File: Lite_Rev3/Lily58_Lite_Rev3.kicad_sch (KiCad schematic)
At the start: 118 parts, among them J1 M2HOLE, J10 LOGO, J10 M2HOLE, J11 LOGO, J11 M2HOLE, J12 HOLE, J13 HOLE, J14 HOLE, J15 HOLE, J16 OLED_R, J19 breakaway, J2 M2HOLE, J20 breakaway, J21 breakaway, J22 AudioJack4, J22 breakaway, J3 HOLE, J4 HOLE, J5 HOLE, J6 HOLE, J7 OLED_L, J9 AudioJack4, SW1 SW_Push, SW10 SW_Push, SW11 SW_Push, SW12 SW_Push, SW13 SW_Push, SW14 SW_Push, SW15 SW_Push, SW16 SW_Push, SW17 SW_Push, SW18 SW_Push, SW19 SW_Push, SW2 SW_Push, SW20 SW_Push, SW21 SW_Push, SW22 SW_Push, SW23 SW_Push, SW24 SW_Push, SW25 SW_Push, SW26 SW_Push, SW27 SW_Push, SW28 SW_Push, SW29 SW_Push, SW3 SW_Push, SW30 SW_Push, SW31 SW_Push, SW32 SW_Push, SW33 SW_Push, SW34 SW_Push, SW35 SW_Push, SW36 SW_Push, SW37 SW_Push, SW38 SW_Push, SW39 SW_Push, SW4 SW_Push, SW40 SW_Push, SW41 SW_Push, SW42 SW_Push, SW43 SW_Push, SW44 SW_Push, SW45 SW_Push, SW46 SW_Push, SW47 SW_Push, SW48 SW_Push, SW49 SW_Push, SW5 SW_Push, SW50 SW_Push, SW51 SW_Push, SW52 SW_Push, SW53 SW_Push, SW54 SW_Push, SW55 SW_Push, SW56 SW_Push, SW57 SW_Push, SW58 SW_Push, SW6 SW_Push, SW7 SW_Push, SW8 SW_Push, SW9 SW_Push

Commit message: [Lily58 Lite Rev3] fix PCB
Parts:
- J12, J13, J14, J15, J3, J4, J5, J6: footprint yuchi:HOLE_M2_TH_5mm -> yuchi:HOLE_M2_TH
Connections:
- net COL4_L: now also SW11.1, SW17.1, SW23.1, SW29.1, SW5.1
- net LED_L_LV: now reaches U1.2 (GP2)
- net LED_R: now reaches U2.2 (GP2)
- no-connect marks 35 -> 33
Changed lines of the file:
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@@
   (title_block
     (title "Lily58 Lite Rev3")
-    (date "2024-09-07")
+    (date "2024-07-18")
   )
   (junction (at 160.02 166.37) (diameter 0) (color 0 0 0 0)
@@
   (no_connect (at 76.2 262.89))
   (no_connect (at 93.98 124.46))
-  (no_connect (at 109.22 162.56))
   (no_connect (at 80.01 46.99))
   (no_connect (at 76.2 170.18))
@@
   (no_connect (at 92.71 243.84))
   (no_connect (at 101.6 243.84))
-  (no_connect (at 113.03 39.37))
   (no_connect (at 85.09 124.46))
   (no_connect (at 93.98 271.78))
@@
     )
   )
+  (global_label "LED_R" (shape input) (at 109.22 162.56 0)
+    (effects (font (size 1.27 1.27)) (justify left))
+    (property "Intersheetrefs" "${INTERSHEET_REFS}" (at 109.22 162.56 0)
+      (effects (font (size 1.27 1.27)) hide)
+    )
+  )
   (global_label "TX_R" (shape input) (at 109.22 160.02 0) (fields_autoplaced)
     (effects (font (size 1.27 1.27)) (justify left))
@@
     )
   )
+  (global_label "COL4_L" (shape input) (at 240.03 34.29 90) (fields_autoplaced)
+    (effects (font (size 1.27 1.27)) (justify left))
+    (property "Intersheetrefs" "${INTERSHEET_REFS}" (at 240.03 24.471 90)
+      (effects (font (size 1.27 1.27)) (justify left) hide)
+    )
+  )
+  (global_label "LED_L_LV" (shape input) (at 113.03 39.37 0)
+    (effects (font (size 1.27 1.27)) (justify left))
+    (property "Intersheetrefs" "${INTERSHEET_REFS}" (at 113.03 39.37 0)
+      (effects (font (size 1.27 1.27)) hide)
+    )
+  )
   (global_label "ROW4_R" (shape input) (at 97.79 189.23 270)
     (effects (font (size 1.27 1.27)) (justify right))
@@
       (effects (font (size 1.27 1.27)) (justify right))
     )
-    (property "Footprint" "yuchi:HOLE_M2_TH_5mm" (at 92.71 238.76 0)
+    (property "Footprint" "yuchi:HOLE_M2_TH" (at 92.71 238.76 0)
       (effects (font (size 1.27 1.27)) hide)
     )
@@
       (effects (font (size 1.27 1.27)) (justify right))
     )
-    (property "Footprint" "yuchi:HOLE_M2_TH_5mm" (at 102.87 119.38 0)
+    (property "Footprint" "yuchi:HOLE_M2_TH" (at 102.87 119.38 0)
       (effects (font (size 1.27 1.27)) hide)
     )
@@
       (effects (font (size 1.27 1.27)) (justify right))
     )
-    (property "Footprint" "yuchi:HOLE_M2_TH_5mm" (at 83.82 238.76 0)
+    (property "Footprint" "yuchi:HOLE_M2_TH" (at 83.82 238.76 0)
       (effects (font (size 1.27 1.27)) hide)
     )
@@
       (effects (font (size 1.27 1.27)) (justify right))
     )
-    (property "Footprint" "yuchi:HOLE_M2_TH_5mm" (at 76.2 119.38 0)
+    (property "Footprint" "yuchi:HOLE_M2_TH" (at 76.2 119.38 0)
       (effects (font (size 1.27 1.27)) hide)
     )
@@
       (effects (font (size 1.27 1.27)) (justify right))
     )
-    (property "Footprint" "yuchi:HOLE_M2_TH_5mm" (at 74.93 238.76 0)
+    (property "Footprint" "yuchi:HOLE_M2_TH" (at 74.93 238.76 0)
       (effects (font (size 1.27 1.27)) hide)
     )
@@
       (effects (font (size 1.27 1.27)) (justify right))
     )
-    (property "Footprint" "yuchi:HOLE_M2_TH_5mm" (at 93.98 119.38 0)
+    (property "Footprint" "yuchi:HOLE_M2_TH" (at 93.98 119.38 0)
       (effects (font (size 1.27 1.27)) hide)
     )
@@
       (effects (font (size 1.27 1.27)) (justify right))
     )
-    (property "Footprint" "yuchi:HOLE_M2_TH_5mm" (at 85.09 119.38 0)
+    (property "Footprint" "yuchi:HOLE_M2_TH" (at 85.09 119.38 0)
       (effects (font (size 1.27 1.27)) hide)
     )
@@
       (effects (font (size 1.27 1.27)) (justify right))
     )
-    (property "Footprint" "yuchi:HOLE_M2_TH_5mm" (at 101.6 238.76 0)
+    (property "Footprint" "yuchi:HOLE_M2_TH" (at 101.6 238.76 0)
       (effects (font (size 1.27 1.27)) hide)
     )

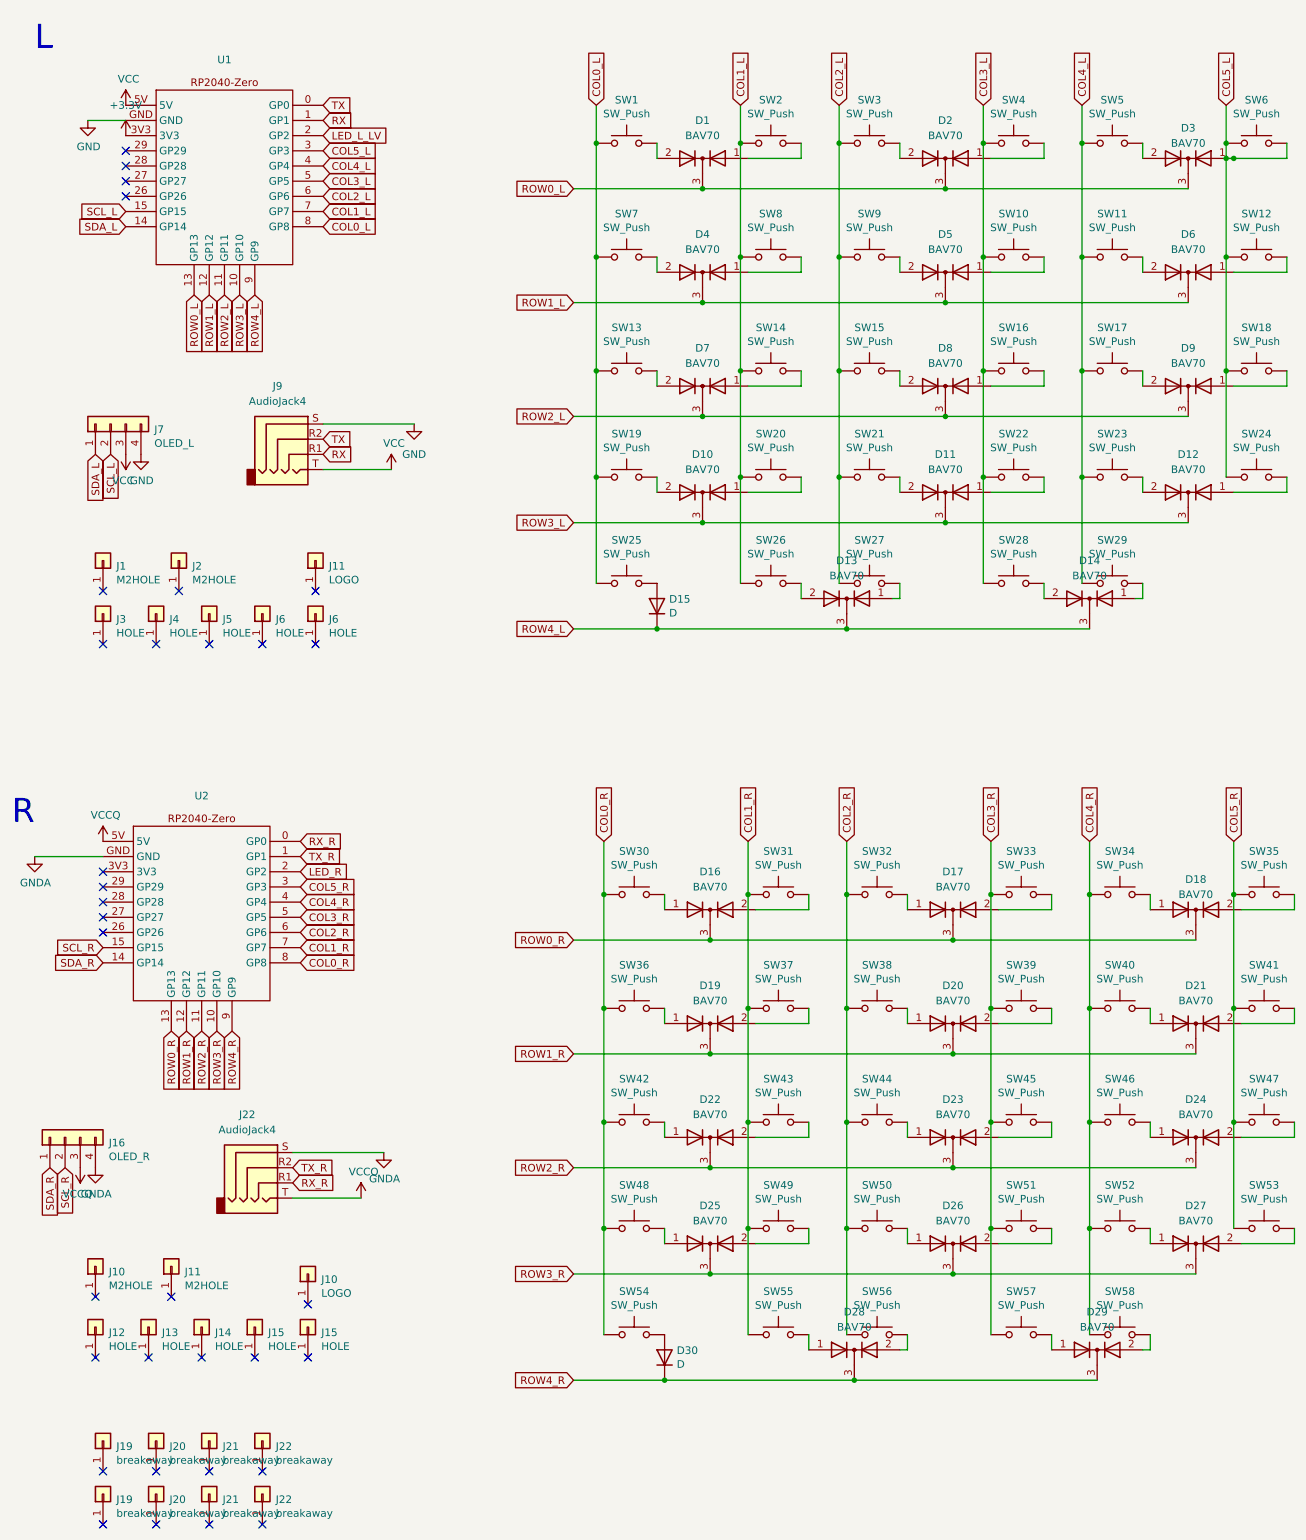
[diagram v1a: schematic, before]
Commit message: [Lily58 Lite Rev3] Fix SW54
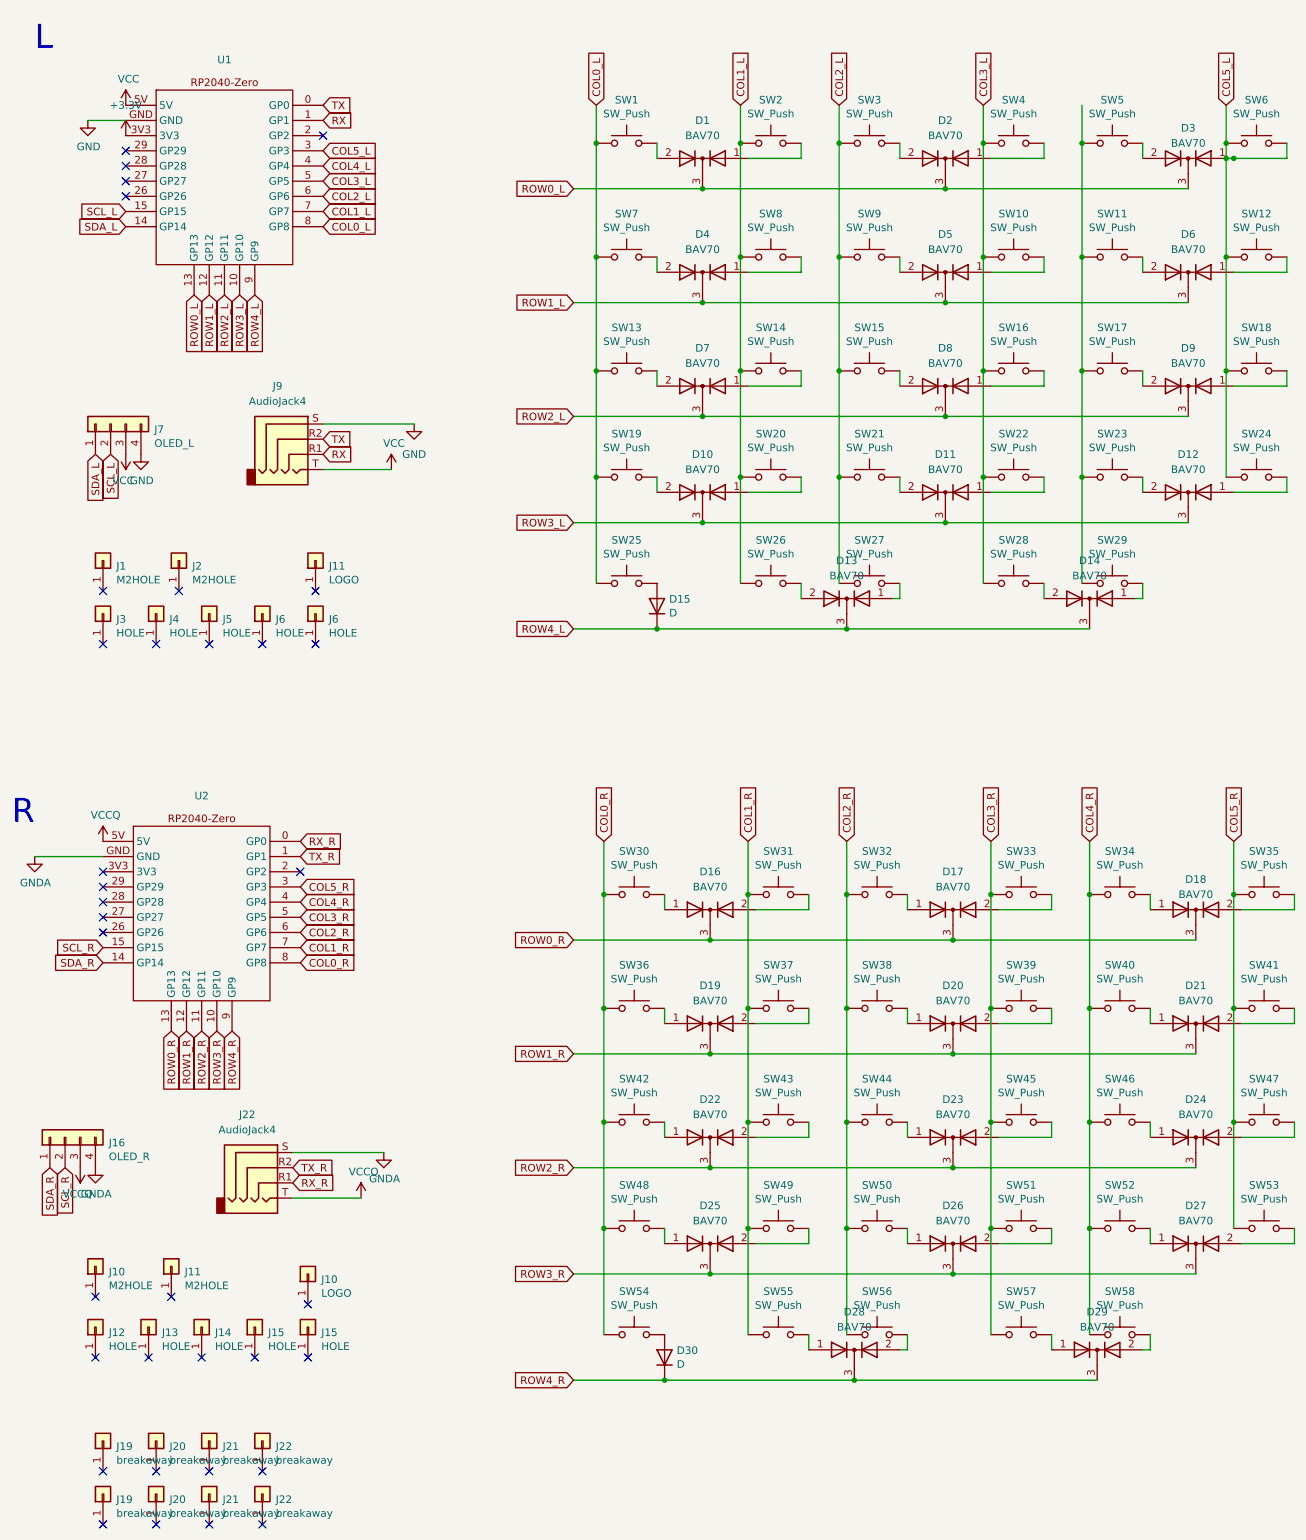
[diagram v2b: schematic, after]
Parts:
- J12, J13, J14, J15, J3, J4, J5, J6: footprint yuchi:HOLE_M2_TH -> yuchi:HOLE_M2_TH_5mm
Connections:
- net COL4_L: no longer SW11.1, SW17.1, SW23.1, SW29.1, SW5.1
- net LED_L_LV: no longer names the net of U1.2 (GP2)
- net LED_R: no longer names the net of U2.2 (GP2)
- new net: SW11.1, SW17.1, SW23.1, SW29.1, SW5.1
- no-connect marks 33 -> 35
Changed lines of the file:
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@@
   (title_block
     (title "Lily58 Lite Rev3")
-    (date "2024-07-18")
+    (date "2024-09-07")
   )
   (junction (at 160.02 166.37) (diameter 0) (color 0 0 0 0)
@@
   (no_connect (at 76.2 262.89))
   (no_connect (at 93.98 124.46))
+  (no_connect (at 109.22 162.56))
   (no_connect (at 80.01 46.99))
   (no_connect (at 76.2 170.18))
@@
   (no_connect (at 92.71 243.84))
   (no_connect (at 101.6 243.84))
+  (no_connect (at 113.03 39.37))
   (no_connect (at 85.09 124.46))
   (no_connect (at 93.98 271.78))
@@
     )
   )
-  (global_label "LED_R" (shape input) (at 109.22 162.56 0)
-    (effects (font (size 1.27 1.27)) (justify left))
-    (property "Intersheetrefs" "${INTERSHEET_REFS}" (at 109.22 162.56 0)
-      (effects (font (size 1.27 1.27)) hide)
-    )
-  )
   (global_label "TX_R" (shape input) (at 109.22 160.02 0) (fields_autoplaced)
     (effects (font (size 1.27 1.27)) (justify left))
@@
     )
   )
-  (global_label "COL4_L" (shape input) (at 240.03 34.29 90) (fields_autoplaced)
-    (effects (font (size 1.27 1.27)) (justify left))
-    (property "Intersheetrefs" "${INTERSHEET_REFS}" (at 240.03 24.471 90)
-      (effects (font (size 1.27 1.27)) (justify left) hide)
-    )
-  )
-  (global_label "LED_L_LV" (shape input) (at 113.03 39.37 0)
-    (effects (font (size 1.27 1.27)) (justify left))
-    (property "Intersheetrefs" "${INTERSHEET_REFS}" (at 113.03 39.37 0)
-      (effects (font (size 1.27 1.27)) hide)
-    )
-  )
   (global_label "ROW4_R" (shape input) (at 97.79 189.23 270)
     (effects (font (size 1.27 1.27)) (justify right))
@@
       (effects (font (size 1.27 1.27)) (justify right))
     )
-    (property "Footprint" "yuchi:HOLE_M2_TH" (at 92.71 238.76 0)
+    (property "Footprint" "yuchi:HOLE_M2_TH_5mm" (at 92.71 238.76 0)
       (effects (font (size 1.27 1.27)) hide)
     )
@@
       (effects (font (size 1.27 1.27)) (justify right))
     )
-    (property "Footprint" "yuchi:HOLE_M2_TH" (at 102.87 119.38 0)
+    (property "Footprint" "yuchi:HOLE_M2_TH_5mm" (at 102.87 119.38 0)
       (effects (font (size 1.27 1.27)) hide)
     )
@@
       (effects (font (size 1.27 1.27)) (justify right))
     )
-    (property "Footprint" "yuchi:HOLE_M2_TH" (at 83.82 238.76 0)
+    (property "Footprint" "yuchi:HOLE_M2_TH_5mm" (at 83.82 238.76 0)
       (effects (font (size 1.27 1.27)) hide)
     )
@@
       (effects (font (size 1.27 1.27)) (justify right))
     )
-    (property "Footprint" "yuchi:HOLE_M2_TH" (at 76.2 119.38 0)
+    (property "Footprint" "yuchi:HOLE_M2_TH_5mm" (at 76.2 119.38 0)
       (effects (font (size 1.27 1.27)) hide)
     )
@@
       (effects (font (size 1.27 1.27)) (justify right))
     )
-    (property "Footprint" "yuchi:HOLE_M2_TH" (at 74.93 238.76 0)
+    (property "Footprint" "yuchi:HOLE_M2_TH_5mm" (at 74.93 238.76 0)
       (effects (font (size 1.27 1.27)) hide)
     )
@@
       (effects (font (size 1.27 1.27)) (justify right))
     )
-    (property "Footprint" "yuchi:HOLE_M2_TH" (at 93.98 119.38 0)
+    (property "Footprint" "yuchi:HOLE_M2_TH_5mm" (at 93.98 119.38 0)
       (effects (font (size 1.27 1.27)) hide)
     )
@@
       (effects (font (size 1.27 1.27)) (justify right))
     )
-    (property "Footprint" "yuchi:HOLE_M2_TH" (at 85.09 119.38 0)
+    (property "Footprint" "yuchi:HOLE_M2_TH_5mm" (at 85.09 119.38 0)
       (effects (font (size 1.27 1.27)) hide)
     )
@@
       (effects (font (size 1.27 1.27)) (justify right))
     )
-    (property "Footprint" "yuchi:HOLE_M2_TH" (at 101.6 238.76 0)
+    (property "Footprint" "yuchi:HOLE_M2_TH_5mm" (at 101.6 238.76 0)
       (effects (font (size 1.27 1.27)) hide)
     )
